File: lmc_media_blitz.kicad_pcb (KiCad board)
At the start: 2 copper layers, 76.2 x 114.3 mm, 79 parts, among them J3 Conn_ARM_JTAG_SWD_10, Q1 BSS138, Q2 BSS138, U1 TPS61222DCK, U10 SK9822, U11 SK9822, U12 SK9822, U13 SK9822, U14 SK9822, U2 TLV77333PDBVR, U3 LPC804M101JDH20, U4 ST25R3918AQW, Y1 27.12MHz

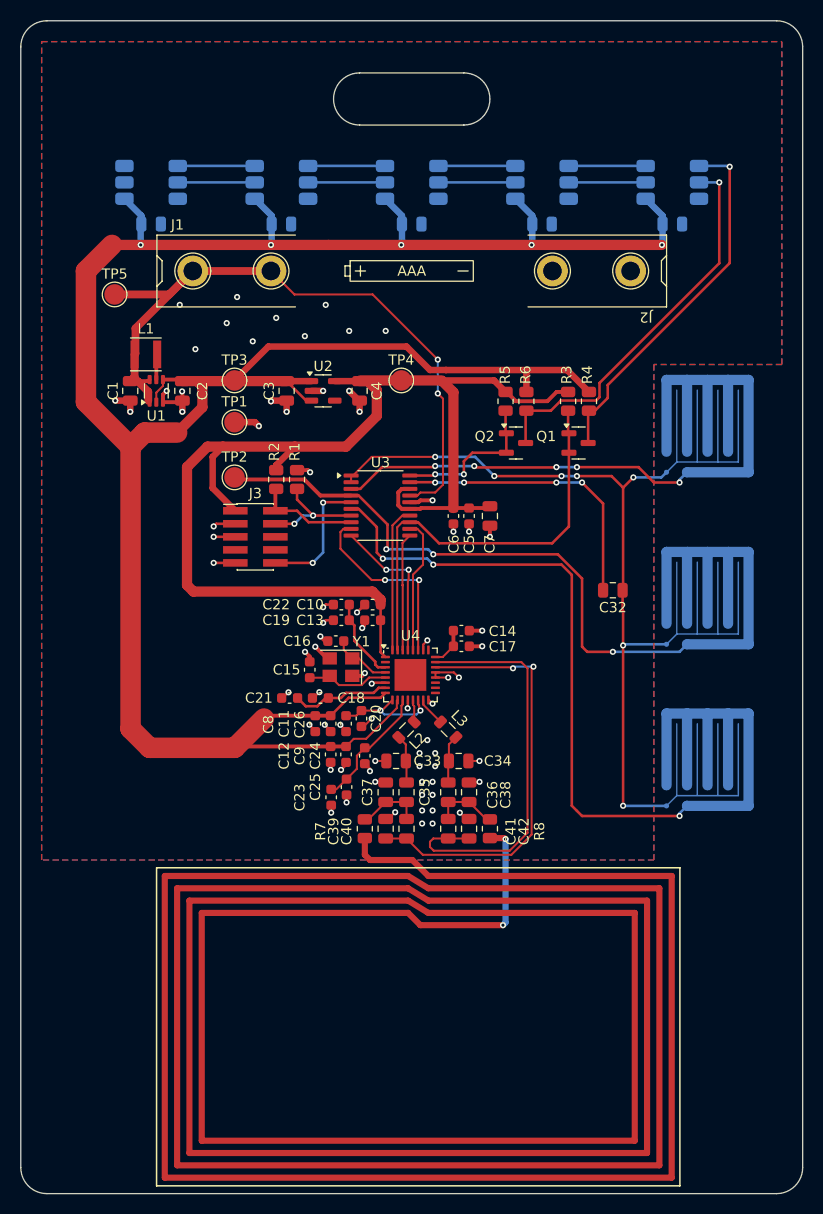
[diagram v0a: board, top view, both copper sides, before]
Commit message: Replaced LPC TSSOP package MCU with QFN package due to unavailability.  Added separate decoupling for analog VDD rail.  Added tooling holes to board for assembly
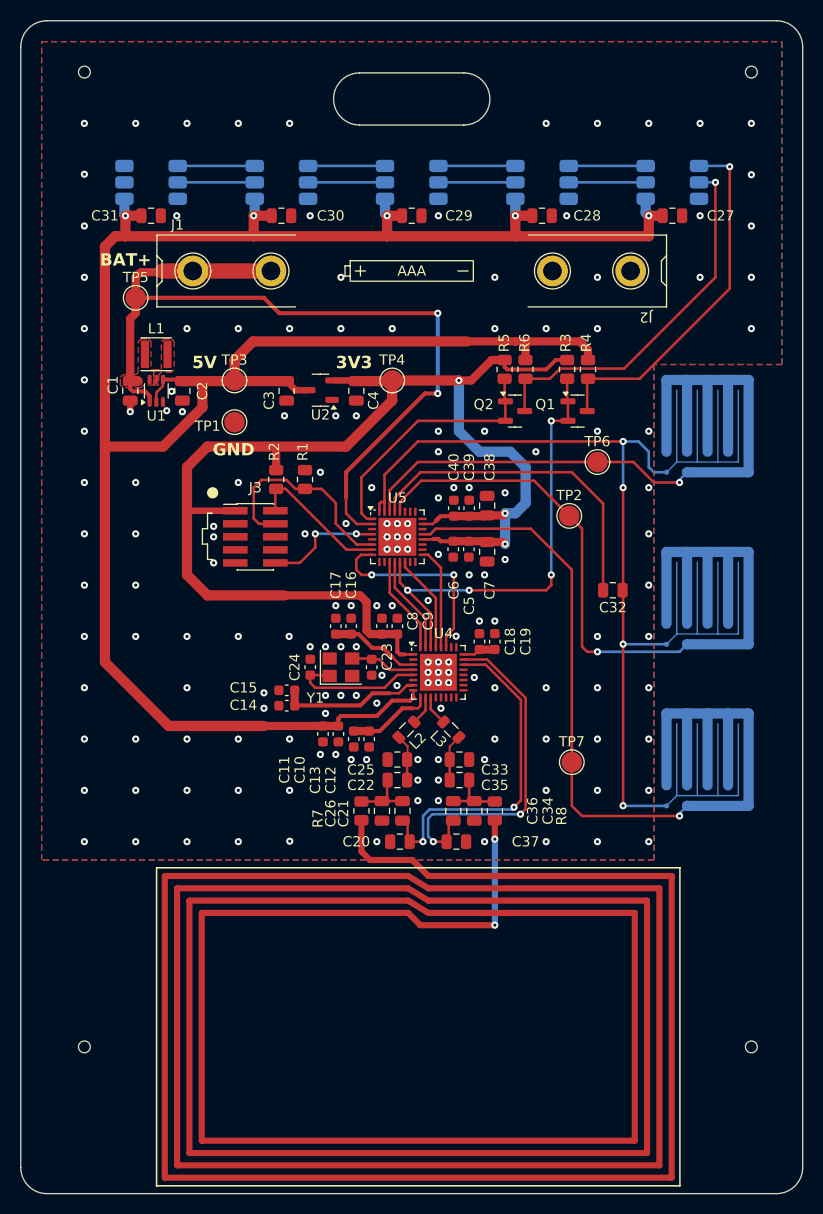
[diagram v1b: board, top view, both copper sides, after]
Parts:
- removed C41, C42: C, Capacitor_SMD:C_0805_2012Metric
- removed U3: LPC804M101JDH20, Package_SO:TSSOP-20_4.4x6.5mm_P0.65mm
- added H1: MountingHole, footprints:JLCPCB_ToolingHole_45.4mils, F.Cu at (185.5, 43.1)
- added H2: MountingHole, footprints:JLCPCB_ToolingHole_45.4mils, F.Cu at (120.5, 43.1)
- added H3: MountingHole, footprints:JLCPCB_ToolingHole_45.4mils, F.Cu at (185.5, 138.1)
- added H4: MountingHole, footprints:JLCPCB_ToolingHole_45.4mils, F.Cu at (120.5, 138.1)
- added TP6: TestPoint_Small, TestPoint:TestPoint_Pad_D2.0mm, F.Cu at (170.5, 81.1)
- added TP7: TestPoint_Small, TestPoint:TestPoint_Pad_D2.0mm, F.Cu at (168.0, 110.3)
- added U5: LPC804M101JHI33, Package_DFN_QFN:QFN-32-1EP_5x5mm_P0.5mm_EP3.7x3.7mm, F.Cu at (151.0, 88.4)
- C10, C14, C9: value 1uF -> 10nF
- C11, C19: value 10nF -> 1uF
- C13, C17: value 10nF -> 2.2uF
- C15: value 15pF -> 2.2uF
- C16: value 15pF -> 10nF
- C20: value 10nF -> 150pF; footprint Capacitor_SMD:C_0603_1608Metric -> Capacitor_SMD:C_0805_2012Metric
- C21: value 2.2uF -> 12pF; footprint Capacitor_SMD:C_0603_1608Metric -> Capacitor_SMD:C_0805_2012Metric
- C22: value 2.2uF -> 100pF; footprint Capacitor_SMD:C_0603_1608Metric -> Capacitor_SMD:C_0805_2012Metric
- C23: value 2.2uF -> 15pF
- C24: value 1nF -> 15pF
- C25: value 10nF -> 470pF; footprint Capacitor_SMD:C_0603_1608Metric -> Capacitor_SMD:C_0805_2012Metric
- C26: value 2.2uF -> 220pF; footprint Capacitor_SMD:C_0603_1608Metric -> Capacitor_SMD:C_0805_2012Metric
- C27, C28, C29, C30, C31: moved to F.Cu
- C33: value C -> 470pF
- C34: value C -> 220pF
- C35: value C -> 100pF
- C36: value C -> 12pF
- C37: value C -> 150pF
- C38: value C -> 10uF
- C39: value C -> 0.1uF; footprint Capacitor_SMD:C_0805_2012Metric -> Capacitor_SMD:C_0603_1608Metric
- C40: value C -> 10nF; footprint Capacitor_SMD:C_0805_2012Metric -> Capacitor_SMD:C_0603_1608Metric
- Q1, Q2: value BSS138 -> 2N7002
- R7, R8: value R -> 1R
- U2: value TLV77333PDBVR -> XC6206PxxxMR; footprint Package_TO_SOT_SMD:SOT-23-5 -> Package_TO_SOT_SMD:SOT-23-3
- U4: value ST25R3918AQW -> ST25R3911B-AQFT; footprint Package_DFN_QFN:HVQFN-32-1EP_5x5mm_P0.5mm_EP3.1x3.1mm -> Package_DFN_QFN:QFN-32-1EP_5x5mm_P0.5mm_EP3.6x3.6mm
- moved TP2 32.8 mm to (167.8, 86.3)
- moved C39 32.3 mm to (158.0, 85.6), turned to 90 degrees
- moved C40 31.6 mm to (156.5, 85.6)
- moved C38 28.0 mm to (159.8, 85.3)
- moved C14 18.5 mm to (140.2, 104.8), turned to 180 degrees
- moved C22 18.0 mm to (151.0, 112.1), turned to 180 degrees
- moved C18 16.4 mm to (159.0, 98.6), turned to 90 degrees
- moved C21 15.6 mm to (151.5, 115.1), turned to 90 degrees
- moved C19 15.1 mm to (160.5, 98.6), turned to 90 degrees
- moved C9 13.5 mm to (151.0, 97.1), turned to 90 degrees
- moved C23 13.3 mm to (148.5, 101.1), turned to -90 degrees
- moved C10 13.0 mm to (145.2, 107.6), turned to -90 degrees
- moved C20 12.6 mm to (151.2, 118.1), turned to 0 degrees
- moved C17 12.4 mm to (145.0, 97.1), turned to -90 degrees
- moved C13 11.7 mm to (146.8, 108.1), turned to 90 degrees
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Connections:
- net Net-(AE1-Pad1) renamed /NFC/ANT_DAMP1
- net Net-(AE1-Pad2) renamed /NFC/ANT_DAMP2
- net Net-(J3-SWCLK/TCK) renamed /SWCLK
- net Net-(J3-SWDIO/TMS) renamed /SWDIO
- net Net-(U1-L) renamed /L
- net Net-(U10-CKO) renamed /LEDs/LED2_CKI
- net Net-(U10-SDO) renamed /LEDs/LED2_SDI
- net Net-(U11-CKO) renamed /LEDs/LED3_CKI
- net Net-(U11-SDO) renamed /LEDs/LED3_SDI
- net Net-(U12-CKO) renamed /LEDs/LED4_CKI
- net Net-(U12-SDO) renamed /LEDs/LED4_SDI
- net Net-(U13-CKO) renamed /LEDs/LED5_CKI
- net Net-(U13-SDO) renamed /LEDs/LED5_SDI
- C10 pad 1: +3V3 -> +5V
- C12 pad 1: +5V -> /NFC/VSP_RF
- C13 pad 1: +3V3 -> GND
- C13 pad 2: GND -> /NFC/VSP_RF
- C14 pad 1: Net-(U4-AGDC) -> /NFC/VSP_A
- C15 pad 1: Net-(U4-XTI) -> GND
- C15 pad 2: GND -> /NFC/VSP_A
- C16 pad 1: Net-(U4-XTO) -> /NFC/VSP_D
- C17 pad 1: Net-(U4-AGDC) -> GND
- C17 pad 2: GND -> /NFC/VSP_D
- C18 pad 1: Net-(U4-VDD_A) -> /NFC/A_REF
- C19 pad 1: Net-(U4-VDD_D) -> /NFC/A_REF
- C20 pad 1: Net-(U4-VDD_DR) -> GND
- C20 pad 2: GND -> /NFC/RFI1
- C21 pad 1: GND -> /NFC/RFI1
- C21 pad 2: Net-(U4-VDD_A) -> /NFC/ANT_MATCH1
- C22 pad 1: GND -> /NFC/ANT_FILT1
- C22 pad 2: Net-(U4-VDD_D) -> /NFC/ANT_MATCH1
- C23 pad 1: GND -> /NFC/XTO
- C23 pad 2: Net-(U4-VDD_AM) -> GND
- C24 pad 1: Net-(U4-VDD_AM) -> /NFC/XTI
- C25 pad 1: Net-(U4-VDD_AM) -> /NFC/ANT_FILT1
- C26 pad 1: GND -> /NFC/ANT_MATCH1
- C26 pad 2: Net-(U4-VDD_DR) -> GND
- C33 pad 1: Net-(C33-Pad1) -> GND
- C33 pad 2: GND -> /NFC/ANT_FILT2
- C34 pad 2: Net-(C34-Pad2) -> /NFC/ANT_MATCH2
- C35 pad 1: Net-(C33-Pad1) -> /NFC/ANT_FILT2
- C35 pad 2: Net-(C35-Pad2) -> /NFC/ANT_MATCH2
- C36 pad 1: Net-(C34-Pad2) -> /NFC/ANT_MATCH2
- C36 pad 2: Net-(C36-Pad2) -> /NFC/RFI2
- C37 pad 1: Net-(C35-Pad2) -> /NFC/RFI2
- C38 pad 2: Net-(C36-Pad2) -> +3V3
- C39 pad 1: GND -> +3V3
- C39 pad 2: Net-(U4-RFI1) -> GND
- C40 pad 1: Net-(U4-RFI1) -> +3V3
- C40 pad 2: Net-(C35-Pad2) -> GND
- C8 pad 1: +5V -> +3V3
- C9 pad 1: +5V -> +3V3
- J3 pad 10: Net-(J3-~{RESET}) -> /nRESET
- L2 pad 1: Net-(U4-RFO1) -> /NFC/RFO1
- L2 pad 2: Net-(C33-Pad1) -> /NFC/ANT_FILT1
- L3 pad 1: Net-(U4-RFO2) -> /NFC/RFO2
- L3 pad 2: Net-(C34-Pad2) -> /NFC/ANT_FILT2
- R7 pad 1: Net-(C35-Pad2) -> /NFC/ANT_MATCH1
- R8 pad 1: Net-(C36-Pad2) -> /NFC/ANT_MATCH2
- U2 pad 1: +5V -> GND
- U2 pad 2: GND -> +3V3
- U4 pad 10: +5V -> /NFC/RFO1
- U4 pad 11: Net-(U4-VDD_AM) -> /NFC/RFO2
- U4 pad 13: Net-(U4-RFO1) -> unconnected-(U4-TRIM1_3-Pad13)
- U4 pad 14: Net-(U4-VDD_DR) -> unconnected-(U4-TRIM2_3-Pad14)
- U4 pad 15: Net-(U4-RFO2) -> unconnected-(U4-TRIM1_2-Pad15)
- U4 pad 16: GND -> unconnected-(U4-TRIM2_2-Pad16)
- U4 pad 20: GND -> unconnected-(U4-TRIM2_0-Pad20)
- U4 pad 22: Net-(U4-RFI1) -> /NFC/RFI1
- U4 pad 23: Net-(U4-RFI2) -> /NFC/RFI2
- U4 pad 24: Net-(U4-AGDC) -> /NFC/A_REF
- U4 pad 29: /SPI0_SSEL0 -> /SPI0_MISO
- U4 pad 3: Net-(U4-VDD_D) -> /NFC/VSP_D
- U4 pad 30: /SPI0_SCKA -> /SPI0_MOSI
- U4 pad 31: /SPI0_MOSI -> /SPI0_SCKA
- U4 pad 32: /SPI0_MISO -> /SPI0_SSEL0
- U4 pad 33: unconnected-(U4-NA-Pad33) -> GND
- U4 pad 4: Net-(U4-XTO) -> /NFC/XTO
- U4 pad 5: Net-(U4-XTI) -> /NFC/XTI
- U4 pad 7: Net-(U4-VDD_A) -> /NFC/VSP_A
- U4 pad 9: Net-(U4-VDD_DR) -> /NFC/VSP_RF
- Y1 pad 1: Net-(U4-XTO) -> /NFC/XTI
- Y1 pad 3: Net-(U4-XTI) -> /NFC/XTO
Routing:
- net GND: track 66.2 -> 1.81 mm, vias 75 -> 167
- net Net-(U4-RFI1): track 41.9 -> 0.00 mm, vias 2 -> 0
- net Net-(U4-RFI2): track 40.5 -> 0.00 mm
- net /NFC/RFI2: track 0.00 -> 34.6 mm, vias 0 -> 2
- net /NFC/RFI1: track 0.00 -> 33.2 mm, vias 0 -> 2
- net +5V: track 247.1 -> 225.4 mm
- net /NFC/VSP_A: track 0.00 -> 15.2 mm
- net +BATT: track 71.0 -> 85.4 mm
- net /NFC/XTI: track 0.00 -> 13.4 mm
- net /CAPT_X1: track 57.0 -> 43.7 mm, vias 3 -> 1
- net Net-(J3-~{RESET}): track 12.7 -> 0.00 mm, vias 2 -> 0
- net Net-(U4-VDD_AM): track 11.7 -> 0.00 mm
- net /nRESET: track 0.00 -> 11.4 mm, vias 0 -> 2
- net Net-(U4-VDD_DR): track 10.5 -> 0.00 mm, vias 2 -> 0
- net +3V3: track 121.0 -> 131.5 mm, vias 0 -> 3
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- added copper zone on F.Cu, net +BATT
- added copper zone on F.Cu, net /L
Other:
- board text added: "3V3"
- board text added: "5V"
- board text added: "BAT+"
- board text added: "GND"

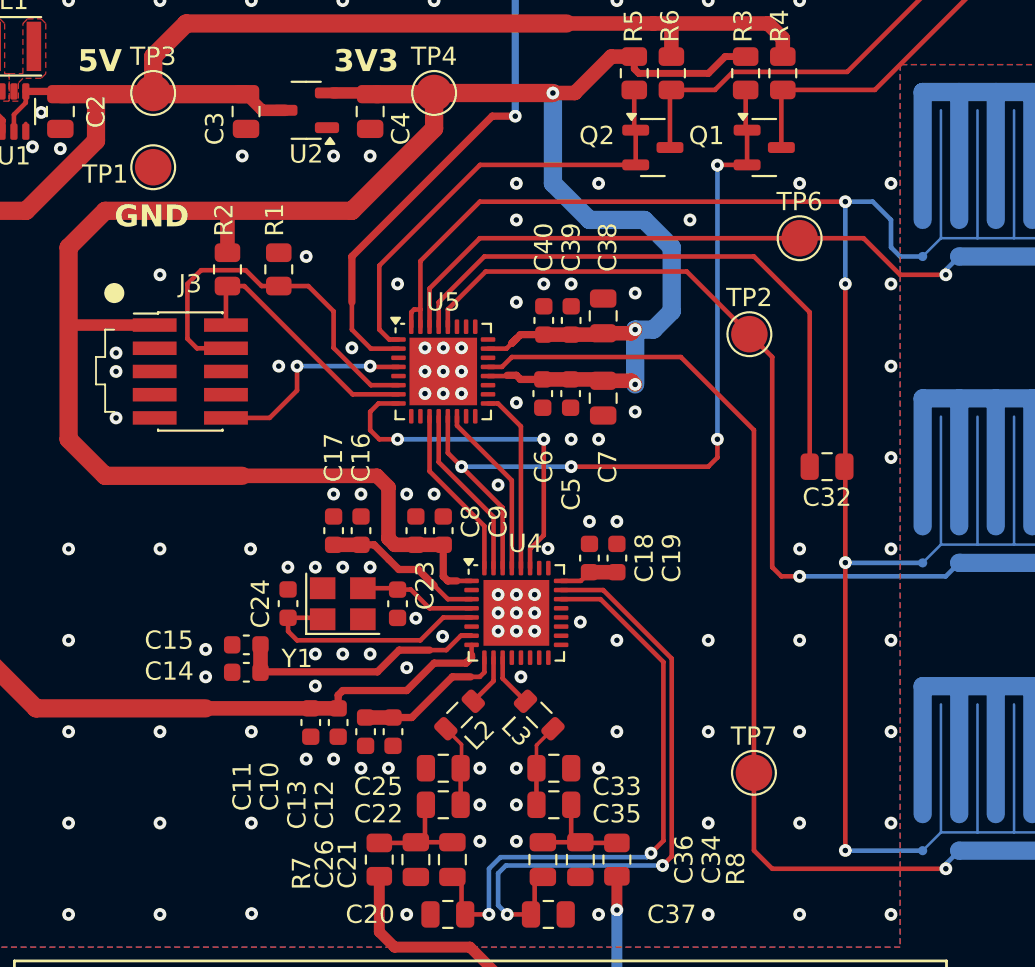
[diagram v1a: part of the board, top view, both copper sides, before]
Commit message: Minor cleanup.  Moved vias to let GND pours flow between islands
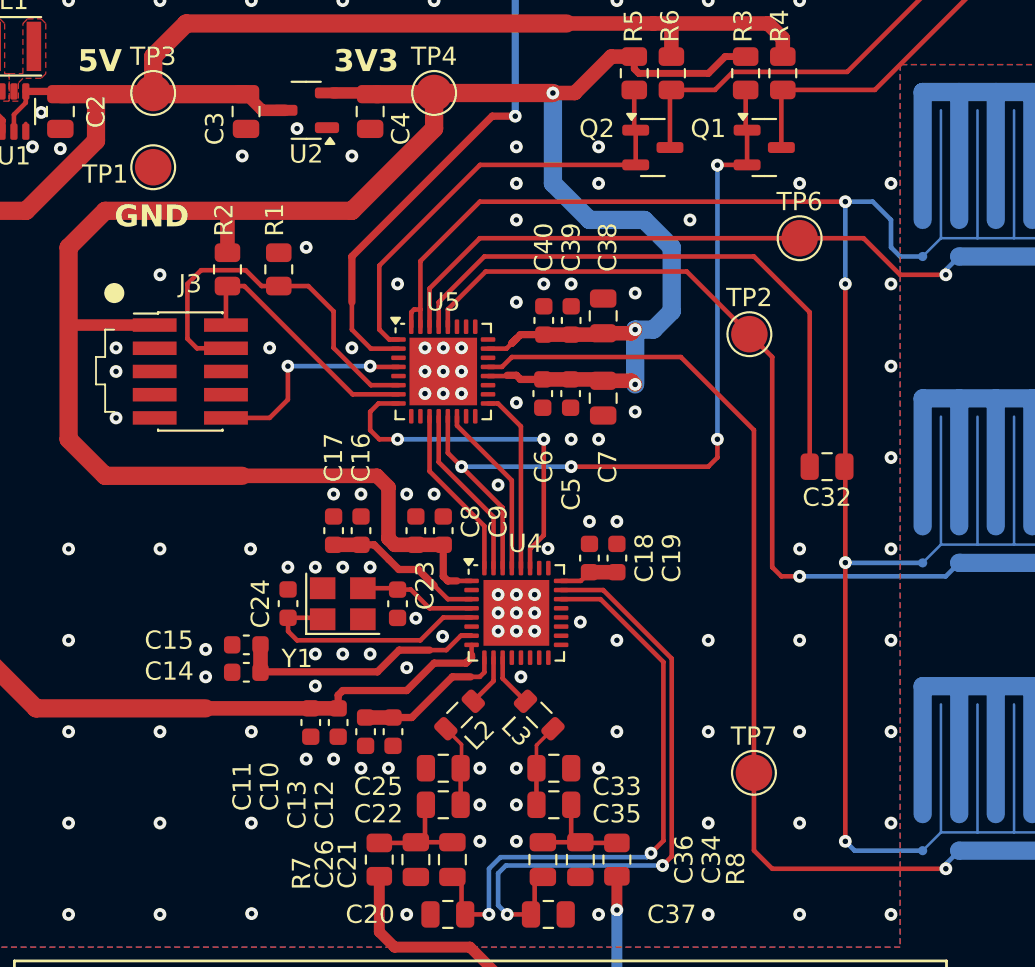
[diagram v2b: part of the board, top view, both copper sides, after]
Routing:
- net GND: vias 167 -> 169
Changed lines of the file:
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@@
 		(tags "SOT TO_SOT_SMD")
 		(property "Reference" "Q2"
-			(at -3.06 -0.648 0)
+			(at -3.06 -1.0365 0)
 			(layer "F.SilkS")
 			(effects
@@
 		(tags "SOT TO_SOT_SMD")
 		(property "Reference" "Q1"
-			(at -3.156 -0.648 0)
+			(at -3.0625 -1.0365 0)
 			(layer "F.SilkS")
 			(effects
@@
 	)
 	(via
-		(at 145 76.6)
+		(at 143 75.1)
 		(size 0.7)
 		(drill 0.3)
@@
 	)
 	(via
-		(at 147 76.6)
+		(at 146 76.6)
 		(size 0.7)
 		(drill 0.3)
@@
 	)
 	(via
-		(at 133.096 87.376)
+		(at 133.096 87.1)
 		(size 0.7)
 		(drill 0.3)
@@
 	)
 	(via
-		(at 143.5 82.1)
+		(at 143.5 81.6)
 		(size 0.7)
 		(drill 0.3)
@@
 	)
 	(via
+		(at 159.5 76.1)
+		(size 0.7)
+		(drill 0.3)
+		(layers "F.Cu" "B.Cu")
+		(net 5)
+	)
+	(via
 		(at 159.5 118.1)
 		(size 0.7)
@@
 	)
 	(via
+		(at 155 76.1)
+		(size 0.7)
+		(drill 0.3)
+		(layers "F.Cu" "B.Cu")
+		(net 5)
+	)
+	(via
 		(at 135.5 98.1)
 		(size 0.7)
@@
 	)
 	(via
-		(at 142 88.1)
+		(at 141.5 87.1)
 		(size 0.7)
 		(drill 0.3)
@@
 	)
 	(segment
-		(start 173 98.85)
-		(end 173 114.6)
-		(width 0.254)
-		(layer "F.Cu")
-		(net 36)
-	)
-	(segment
 		(start 149.25 85.942)
 		(end 149.25 85.15)
@@
 	)
 	(segment
+		(start 173 98.85)
+		(end 173 114.1)
+		(width 0.254)
+		(layer "F.Cu")
+		(net 36)
+	)
+	(segment
 		(start 153 79.1)
 		(end 149.75 82.35)
@@
 	)
 	(via
-		(at 173 114.6)
+		(at 173 114.1)
 		(size 0.7)
 		(drill 0.3)
@@
 	)
 	(segment
-		(start 173 114.6)
-		(end 173.011 114.611)
+		(start 173 114.1)
+		(end 173.511 114.611)
 		(width 0.254)
 		(layer "B.Cu")
@@
 	)
 	(segment
+		(start 173.511 114.611)
+		(end 177.231 114.611)
+		(width 0.254)
+		(layer "B.Cu")
+		(net 36)
+	)
+	(segment
 		(start 173 79.1)
 		(end 174.5 79.1)
@@
 	)
 	(segment
-		(start 173.011 114.611)
-		(end 177.231 114.611)
-		(width 0.254)
-		(layer "B.Cu")
-		(net 36)
-	)
-	(segment
 		(start 173 98.85)
 		(end 173.097 98.85)
@@
 	)
 	(segment
-		(start 143 88.1)
-		(end 143 89.432)
+		(start 142.5 88.1)
+		(end 142.5 89.932)
 		(width 0.254)
 		(layer "F.Cu")
@@
 	)
 	(segment
-		(start 143 89.432)
-		(end 141.5 90.932)
-		(width 0.254)
+		(start 147.042 88.142)
+		(end 147 88.1)
+		(width 0.2)
 		(layer "F.Cu")
 		(net 37)
 	)
 	(segment
-		(start 147.042 88.142)
-		(end 147 88.1)
-		(width 0.2)
+		(start 141.5 90.932)
+		(end 139.11 90.932)
+		(width 0.254)
 		(layer "F.Cu")
 		(net 37)
@@
 	)
 	(segment
-		(start 141.5 90.932)
-		(end 139.11 90.932)
+		(start 142.5 89.932)
+		(end 141.5 90.932)
 		(width 0.254)
 		(layer "F.Cu")
@@
 	)
 	(via
-		(at 143 88.1)
+		(at 142.5 88.1)
 		(size 0.7)
 		(drill 0.3)
@@
 	(segment
 		(start 147 88.1)
-		(end 143 88.1)
+		(end 142.5 88.1)
 		(width 0.254)
 		(layer "B.Cu")
@@
 		(polygon
 			(pts
-				(xy 127.25 73.6) (xy 127.25 72.85) (xy 127.25 72.1) (xy 128 72.1) (xy 128 72.1) (xy 128 69.35) (xy 128.25 69.1)
+				(xy 127.25 73.6) (xy 127.25 72.85) (xy 127.25 72.1) (xy 128 72.1) (xy 128 69.35) (xy 128.25 69.1)
 				(xy 129 69.1) (xy 129.25 69.35) (xy 129.25 72.1) (xy 129 72.35) (xy 128 72.35) (xy 127.75 72.6)
 				(xy 127.75 73.6)
